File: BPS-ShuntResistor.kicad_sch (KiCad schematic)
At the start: 15 parts, among them J3 Amp_Conn

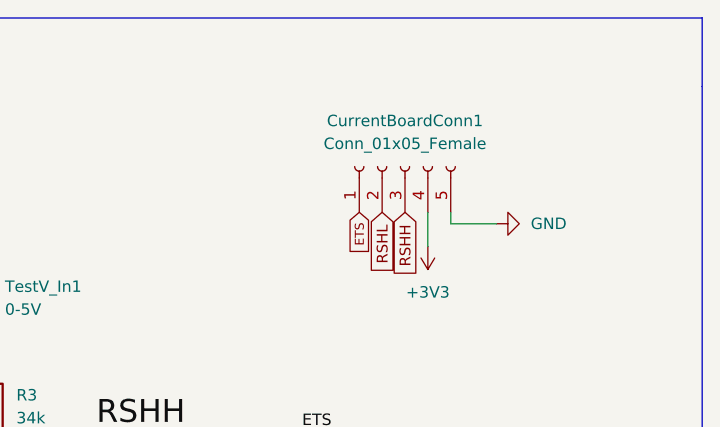
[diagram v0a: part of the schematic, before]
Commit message: Updated BOM csv with approximate prices and potential Mouser lists
Ignore PCB update, footprint for 1x5 connector not decided
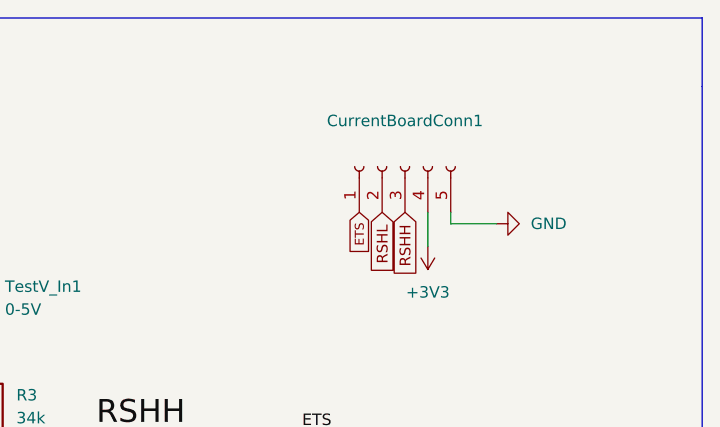
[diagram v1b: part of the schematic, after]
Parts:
- CurrentBoardConn1: value Conn_01x05_Female -> (none); footprint Connector_PinSocket_2.54mm:PinSocket_1x05_P2.54mm_Vertical -> (none)
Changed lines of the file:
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@@
     (in_bom yes) (on_board yes) (fields_autoplaced)
     (property "Reference" "CurrentBoardConn1" (id 0) (at 199.39 71.12 90))
-    (property "Value" "Conn_01x05_Female" (id 1) (at 199.39 73.66 90))
-    (property "Footprint" "Connector_PinSocket_2.54mm:PinSocket_1x05_P2.54mm_Vertical" (id 2) (at 199.39 76.2 0)
+    (property "Value" "" (id 1) (at 199.39 73.66 90))
+    (property "Footprint" "" (id 2) (at 199.39 76.2 0)
       (effects (font (size 1.27 1.27)) hide)
     )
-    (property "Datasheet" "https://www.mouser.com/datasheet/2/418/8/ENG_CD_534237_S-2408977.pdf" (id 3) (at 199.39 76.2 0)
+    (property "Datasheet" "https://www.mouser.com/datasheet/2/276/2/2078430005_PCB_HEADERS-1912713.pdf" (id 3) (at 199.39 76.2 0)
       (effects (font (size 1.27 1.27)) hide)
     )
@@
     )
     (path "/4f59afea-52a6-42ef-a827-b3f6d4652563"
-      (reference "CurrentBoardConn1") (unit 1) (value "Conn_01x05_Female") (footprint "Connector_PinSocket_2.54mm:PinSocket_1x05_P2.54mm_Vertical")
+      (reference "CurrentBoardConn1") (unit 1) (value "Conn_01x05_Male") (footprint "Connector_Molex:Molex_CLIK-Mate_502443-0570_1x05-1MP_P2.00mm_Vertical")
     )
     (path "/3572c1b1-2f58-437c-82f9-d5a67fadda96"

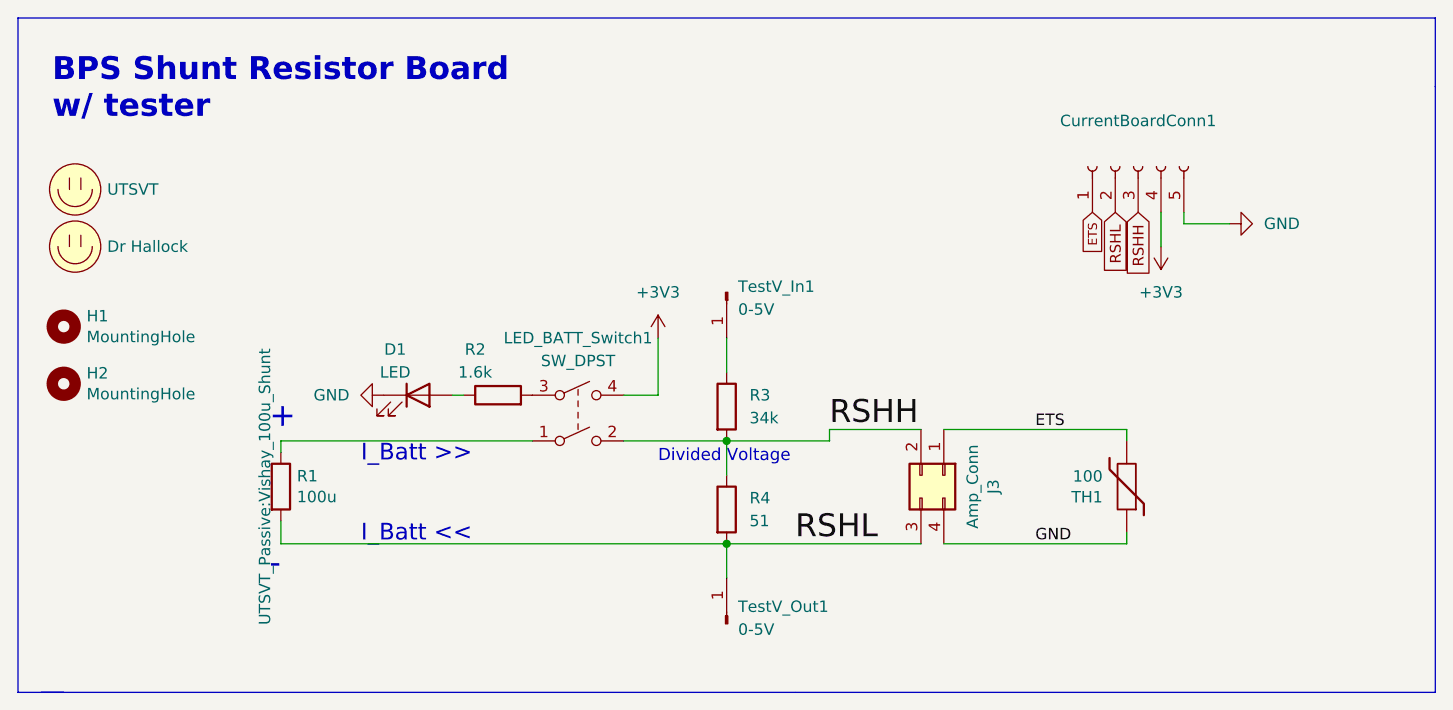
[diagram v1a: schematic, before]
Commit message: Update BPS-ShuntResistor.kicad_sch
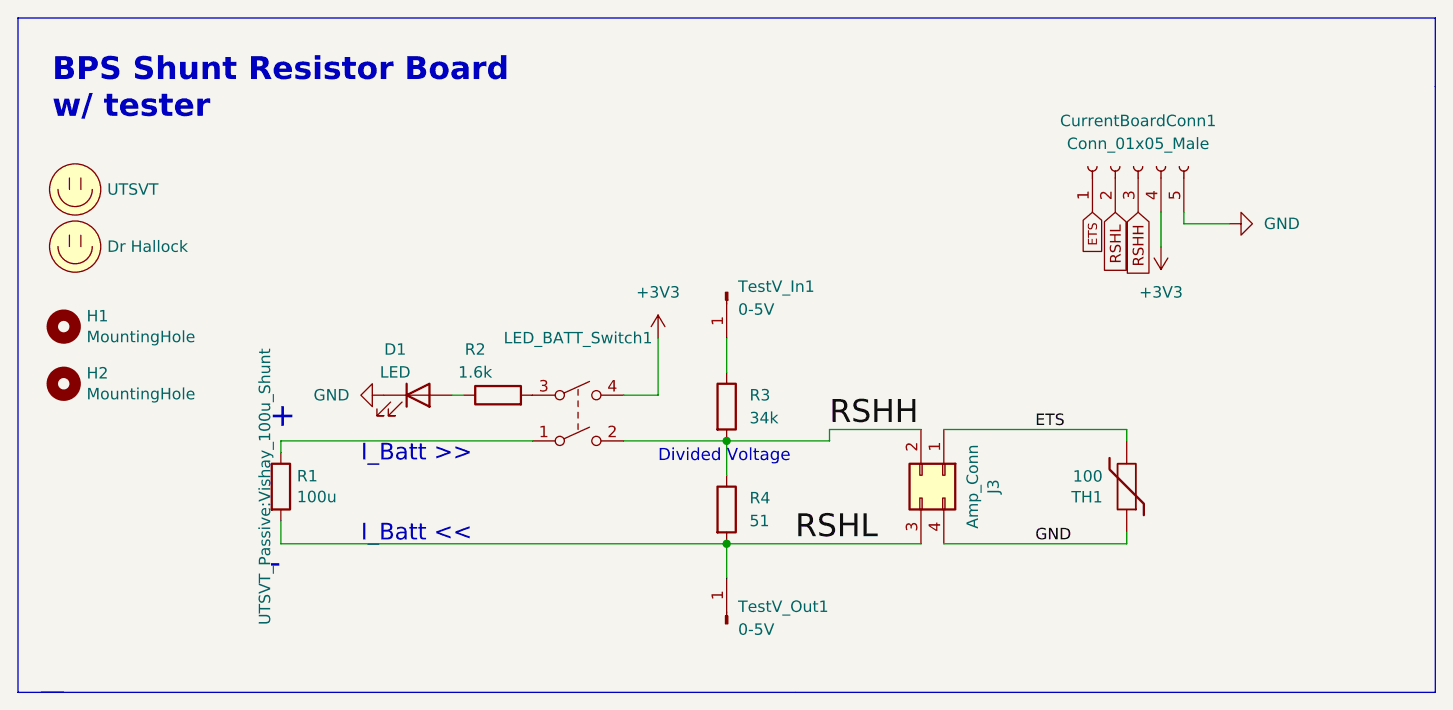
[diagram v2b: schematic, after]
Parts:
- CurrentBoardConn1: value (none) -> Conn_01x05_Male; footprint (none) -> Connector_Molex:Molex_CLIK-Mate_502443-0570_1x05-1MP_P2.00mm_Vertical
- LED_BATT_Switch1: value SW_DPST -> (none); footprint UTSVT_Passive:SW_PVA1EEH1 -> (none)
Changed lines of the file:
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@@
     (in_bom yes) (on_board yes) (fields_autoplaced)
     (property "Reference" "CurrentBoardConn1" (id 0) (at 199.39 71.12 90))
-    (property "Value" "" (id 1) (at 199.39 73.66 90))
-    (property "Footprint" "" (id 2) (at 199.39 76.2 0)
+    (property "Value" "Conn_01x05_Male" (id 1) (at 199.39 73.66 90))
+    (property "Footprint" "Connector_Molex:Molex_CLIK-Mate_502443-0570_1x05-1MP_P2.00mm_Vertical" (id 2) (at 199.39 76.2 0)
       (effects (font (size 1.27 1.27)) hide)
     )
@@
     (in_bom yes) (on_board yes) (fields_autoplaced)
     (property "Reference" "LED_BATT_Switch1" (id 0) (at 137.16 95.25 0))
-    (property "Value" "SW_DPST" (id 1) (at 137.16 97.79 0))
-    (property "Footprint" "UTSVT_Passive:SW_PVA1EEH1" (id 2) (at 137.16 104.14 0)
+    (property "Value" "" (id 1) (at 137.16 97.79 0))
+    (property "Footprint" "" (id 2) (at 137.16 104.14 0)
       (effects (font (size 1.27 1.27)) hide)
     )

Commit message: Update BPS-ShuntResistor.kicad_sch
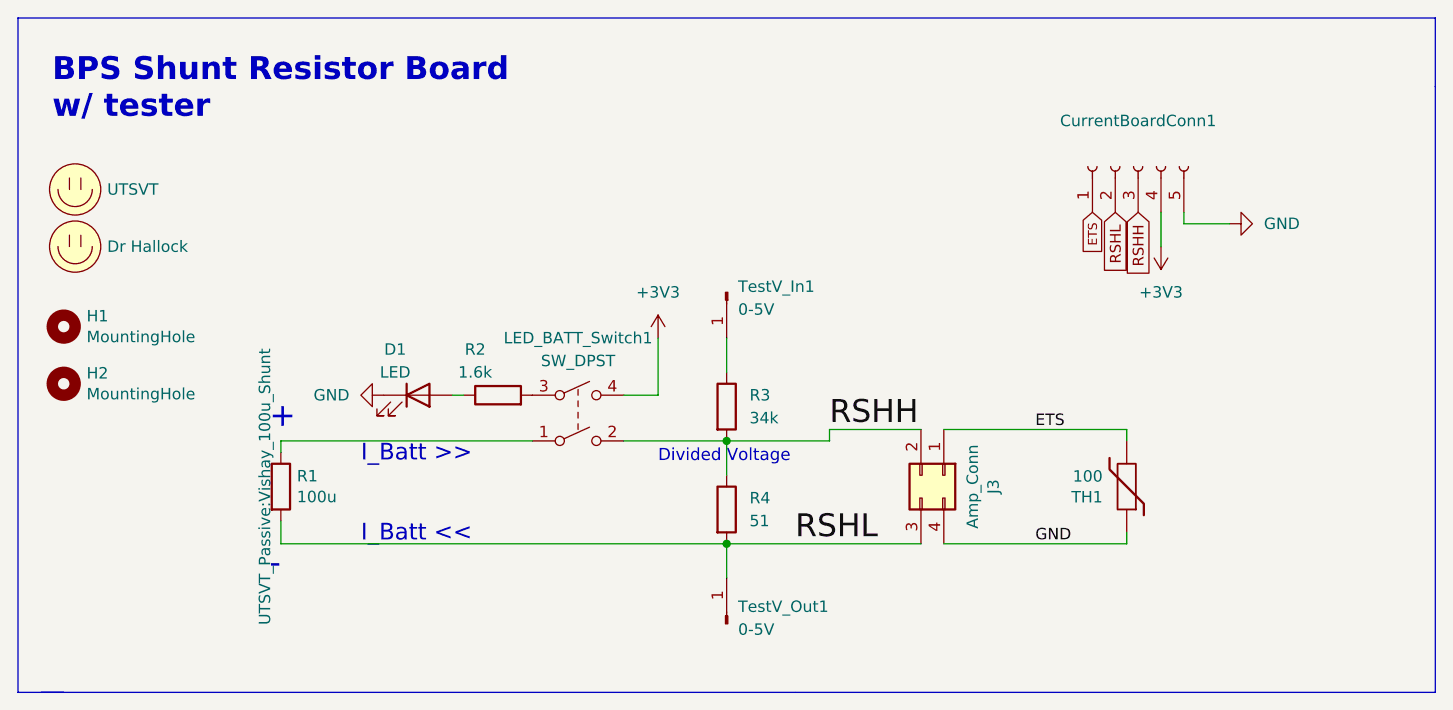
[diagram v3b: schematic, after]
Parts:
- CurrentBoardConn1: value Conn_01x05_Male -> (none); footprint Connector_Molex:Molex_CLIK-Mate_502443-0570_1x05-1MP_P2.00mm_Vertical -> (none)
- LED_BATT_Switch1: value (none) -> SW_DPST; footprint (none) -> UTSVT_Passive:SW_PVA1EEH1
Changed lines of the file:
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@@
     (in_bom yes) (on_board yes) (fields_autoplaced)
     (property "Reference" "CurrentBoardConn1" (id 0) (at 199.39 71.12 90))
-    (property "Value" "Conn_01x05_Male" (id 1) (at 199.39 73.66 90))
-    (property "Footprint" "Connector_Molex:Molex_CLIK-Mate_502443-0570_1x05-1MP_P2.00mm_Vertical" (id 2) (at 199.39 76.2 0)
+    (property "Value" "" (id 1) (at 199.39 73.66 90))
+    (property "Footprint" "" (id 2) (at 199.39 76.2 0)
       (effects (font (size 1.27 1.27)) hide)
     )
-    (property "Datasheet" "https://www.mouser.com/datasheet/2/276/2/2078430005_PCB_HEADERS-1912713.pdf" (id 3) (at 199.39 76.2 0)
+    (property "Datasheet" "generic fella" (id 3) (at 199.39 76.2 0)
       (effects (font (size 1.27 1.27)) hide)
     )
@@
     (in_bom yes) (on_board yes) (fields_autoplaced)
     (property "Reference" "LED_BATT_Switch1" (id 0) (at 137.16 95.25 0))
-    (property "Value" "" (id 1) (at 137.16 97.79 0))
-    (property "Footprint" "" (id 2) (at 137.16 104.14 0)
+    (property "Value" "SW_DPST" (id 1) (at 137.16 97.79 0))
+    (property "Footprint" "UTSVT_Passive:SW_PVA1EEH1" (id 2) (at 137.16 104.14 0)
       (effects (font (size 1.27 1.27)) hide)
     )
@@
     )
     (path "/4f59afea-52a6-42ef-a827-b3f6d4652563"
-      (reference "CurrentBoardConn1") (unit 1) (value "Conn_01x05_Male") (footprint "Connector_Molex:Molex_CLIK-Mate_502443-0570_1x05-1MP_P2.00mm_Vertical")
+      (reference "CurrentBoardConn1") (unit 1) (value "Conn_01x05_Male") (footprint "Connector_PinHeader_2.54mm:PinHeader_1x05_P2.54mm_Vertical")
     )
     (path "/3572c1b1-2f58-437c-82f9-d5a67fadda96"

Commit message: Working on new layout
Kind of messy
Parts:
- CurrentBoardConn1: value (none) -> Conn_01x05_Male; footprint (none) -> Connector_PinHeader_2.54mm:PinHeader_1x05_P2.54mm_Vertical
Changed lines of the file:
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@@
     (in_bom yes) (on_board yes) (fields_autoplaced)
     (property "Reference" "CurrentBoardConn1" (id 0) (at 199.39 71.12 90))
-    (property "Value" "" (id 1) (at 199.39 73.66 90))
-    (property "Footprint" "" (id 2) (at 199.39 76.2 0)
+    (property "Value" "Conn_01x05_Male" (id 1) (at 199.39 73.66 90))
+    (property "Footprint" "Connector_PinHeader_2.54mm:PinHeader_1x05_P2.54mm_Vertical" (id 2) (at 199.39 76.2 0)
       (effects (font (size 1.27 1.27)) hide)
     )

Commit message: working on it
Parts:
- removed LED_BATT_Switch1: SW_DPST, UTSVT_Passive:SW_PVA1EEH1, symbol Switch:SW_DPST
- added SW1: (no value), symbol Switch:SW_DPST
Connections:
- net +3V3: now also SW1.4
- net RSHH: now also SW1.2
- net at R1.1: now also SW1.1
- net at R2.2: now also SW1.3
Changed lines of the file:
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@@
+    (pin "4")
+  )
+  (symbol (lib_id "Switch:SW_DPST") (at 137.16 104.14 0) (unit 1)
+    (in_bom yes) (on_board yes) (fields_autoplaced)
+    (property "Reference" "SW1" (id 0) (at 137.16 95.25 0))
+    (property "Value" "" (id 1) (at 137.16 97.79 0))
+    (property "Footprint" "" (id 2) (at 137.16 104.14 0)
+      (effects (font (size 1.27 1.27)) hide)
+    )
+    (property "Datasheet" "https://www.mouser.com/datasheet/2/15/SDDJE-1370828.pdf" (id 3) (at 137.16 104.14 0)
+      (effects (font (size 1.27 1.27)) hide)
+    )
+    (pin "1")
+    (pin "2")
+    (pin "3")
     (pin "4")
   )
@@
     (pin "5")
   )
-  (symbol (lib_id "Switch:SW_DPST") (at 137.16 104.14 0) (unit 1)
-    (in_bom yes) (on_board yes) (fields_autoplaced)
-    (property "Reference" "LED_BATT_Switch1" (id 0) (at 137.16 95.25 0))
-    (property "Value" "SW_DPST" (id 1) (at 137.16 97.79 0))
-    (property "Footprint" "UTSVT_Passive:SW_PVA1EEH1" (id 2) (at 137.16 104.14 0)
-      (effects (font (size 1.27 1.27)) hide)
-    )
-    (property "Datasheet" "https://www.mouser.com/datasheet/2/57/A_Toggle_Switch-1600832.pdf" (id 3) (at 137.16 104.14 0)
-      (effects (font (size 1.27 1.27)) hide)
-    )
-    (pin "1")
-    (pin "2")
-    (pin "3")
-    (pin "4")
-  )
   (symbol (lib_id "power:GND") (at 209.55 82.55 90) (unit 1)
     (in_bom yes) (on_board yes) (fields_autoplaced)
@@
       (reference "J3") (unit 1) (value "Amp_Conn") (footprint "UTSVT_Connectors:Power_Metal_Strip_Battery_Shunt_Resistor_4_Pin_Connector")
     )
-    (path "/6248ffc4-1f0b-43af-8e3a-5fbfccd4f2e0"
-      (reference "LED_BATT_Switch1") (unit 1) (value "SW_DPST") (footprint "UTSVT_Passive:SW_PVA1EEH1")
-    )
     (path "/00000000-0000-0000-0000-00005f53fe42"
       (reference "LOGO1") (unit 1) (value "UTSVT") (footprint "UTSVT_Special:UTSVT_Logo_Symbol")
@@
       (reference "R4") (unit 1) (value "51") (footprint "Resistor_SMD:R_0805_2012Metric")
     )
+    (path "/0523687d-21a1-4102-9e2f-f501f096d405"
+      (reference "SW1") (unit 1) (value "SW_DPST") (footprint "UTSVT_Special:SDDJE32700")
+    )
     (path "/bff0be5b-fcea-4d1b-a22e-58c65723f733"

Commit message: still working on layout.
i want to double check some footprints.
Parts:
- added TP1, TP2, TP3: TestPoint, TestPoint:TestPoint_Keystone_5005-5009_Compact, symbol Connector:TestPoint
- SW1: value (none) -> SW_DPST; footprint (none) -> UTSVT_Special:SDDJE32700
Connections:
- net +3V3: now also CurrentBoardConn1.5 (Pin_5), TP1.1; no longer CurrentBoardConn1.4 (Pin_4)
- net GND: now also CurrentBoardConn1.4 (Pin_4); no longer CurrentBoardConn1.5 (Pin_5)
- net RSHH: now also CurrentBoardConn1.2 (Pin_2), TP3.1; no longer CurrentBoardConn1.3 (Pin_3)
- net RSHL: now also CurrentBoardConn1.3 (Pin_3), TP2.1; no longer CurrentBoardConn1.2 (Pin_2)

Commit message: Update BPS-ShuntResistor.kicad_sch
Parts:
- removed SW1: SW_DPST, UTSVT_Special:SDDJE32700, symbol Switch:SW_DPST
- added SW?: (no value), symbol Switch:SW_DPST
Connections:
- net +3V3: now also SW?.4
- net RSHH: now also SW?.2
- net at R1.1: now also SW?.1
- net at R2.2: now also SW?.3
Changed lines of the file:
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@@
-    (pin "4")
-  )
-  (symbol (lib_id "Switch:SW_DPST") (at 137.16 104.14 0) (unit 1)
-    (in_bom yes) (on_board yes) (fields_autoplaced)
-    (property "Reference" "SW1" (id 0) (at 137.16 95.25 0))
-    (property "Value" "SW_DPST" (id 1) (at 137.16 97.79 0))
-    (property "Footprint" "UTSVT_Special:SDDJE32700" (id 2) (at 137.16 104.14 0)
-      (effects (font (size 1.27 1.27)) hide)
-    )
-    (property "Datasheet" "https://www.mouser.com/datasheet/2/15/SDDJE-1370828.pdf" (id 3) (at 137.16 104.14 0)
-      (effects (font (size 1.27 1.27)) hide)
-    )
-    (pin "1")
-    (pin "2")
-    (pin "3")
     (pin "4")
   )
@@
     (pin "1")
   )
+  (symbol (lib_id "Switch:SW_DPST") (at 137.16 104.14 0) (unit 1)
+    (in_bom yes) (on_board yes) (fields_autoplaced)
+    (property "Reference" "SW?" (id 0) (at 137.16 95.25 0))
+    (property "Value" "" (id 1) (at 137.16 97.79 0))
+    (property "Footprint" "" (id 2) (at 137.16 104.14 0)
+      (effects (font (size 1.27 1.27)) hide)
+    )
+    (property "Datasheet" "https://www.mouser.com/ProductDetail/CTS-Electronic-Components/206-212?qs=Mr%252BgrRYddfqmzbod607M8A%3D%3D" (id 3) (at 137.16 104.14 0)
+      (effects (font (size 1.27 1.27)) hide)
+    )
+    (pin "1")
+    (pin "2")
+    (pin "3")
+    (pin "4")
+  )
   (symbol (lib_id "Connector:Conn_01x01_Male") (at 153.67 90.17 270) (unit 1)
     (in_bom yes) (on_board yes) (fields_autoplaced)
@@
       (reference "R4") (unit 1) (value "51") (footprint "Resistor_SMD:R_0805_2012Metric")
     )
-    (path "/0523687d-21a1-4102-9e2f-f501f096d405"
-      (reference "SW1") (unit 1) (value "SW_DPST") (footprint "UTSVT_Special:SDDJE32700")
+    (path "/752b3695-5f89-4c59-a33a-3588ae69b756"
+      (reference "SW?") (unit 1) (value "SW_DPST") (footprint "")
     )
     (path "/bff0be5b-fcea-4d1b-a22e-58c65723f733"

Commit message: updating custom board parts
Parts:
- gave numbers to parts that had none: 1
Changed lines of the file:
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@@
   (symbol (lib_id "Switch:SW_DPST") (at 137.16 104.14 0) (unit 1)
     (in_bom yes) (on_board yes) (fields_autoplaced)
-    (property "Reference" "SW?" (id 0) (at 137.16 95.25 0))
+    (property "Reference" "SW1" (id 0) (at 137.16 95.25 0))
     (property "Value" "" (id 1) (at 137.16 97.79 0))
     (property "Footprint" "" (id 2) (at 137.16 104.14 0)
@@
     )
     (path "/752b3695-5f89-4c59-a33a-3588ae69b756"
-      (reference "SW?") (unit 1) (value "SW_DPST") (footprint "")
+      (reference "SW1") (unit 1) (value "SW_DPST") (footprint "UTSVT_Special:206212")
     )
     (path "/bff0be5b-fcea-4d1b-a22e-58c65723f733"
